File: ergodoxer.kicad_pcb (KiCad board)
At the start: 2 copper layers, 197.9 x 173.2 mm, 163 parts, among them J1 USB_C_Receptacle, SW1 SW_Push_mod, SW10 SW_Push, SW11 SW_Push, SW12 SW_Push, SW13 SW_Push_mod, SW14 SW_Push, SW15 SW_Push, SW16 SW_Push, SW17 SW_Push, SW18 SW_Push, SW19 SW_Push_mod, SW2 SW_Push, SW20 SW_Push, SW21 SW_Push, SW22 SW_Push, SW23 SW_Push, SW24 SW_Push, SW25 SW_Push_mod, SW26 SW_Push, SW27 SW_Push, SW28 SW_Push, SW29 SW_Push, SW3 SW_Push, SW30 SW_Push, SW31 SW_Push_mod, SW32 SW_Push, SW33 SW_Push, SW34 SW_Push, SW35 SW_Push, SW37 SW_Push_mod, SW38 SW_Push, SW39 SW_Push, SW4 SW_Push, SW40 SW_Push, SW41 SW_Push, SW43 SW_Push, SW45 SW_Push, SW46 SW_Push, SW48 SW_Push, SW49 SW_Push, SW5 SW_Push, SW50 SW_Push, SW51 SW_Push, SW52 SW_Push, SW53 SW_Push, SW6 SW_Push, SW7 SW_Push_mod, SW8 SW_Push, SW9 SW_Push, U1 proton_c

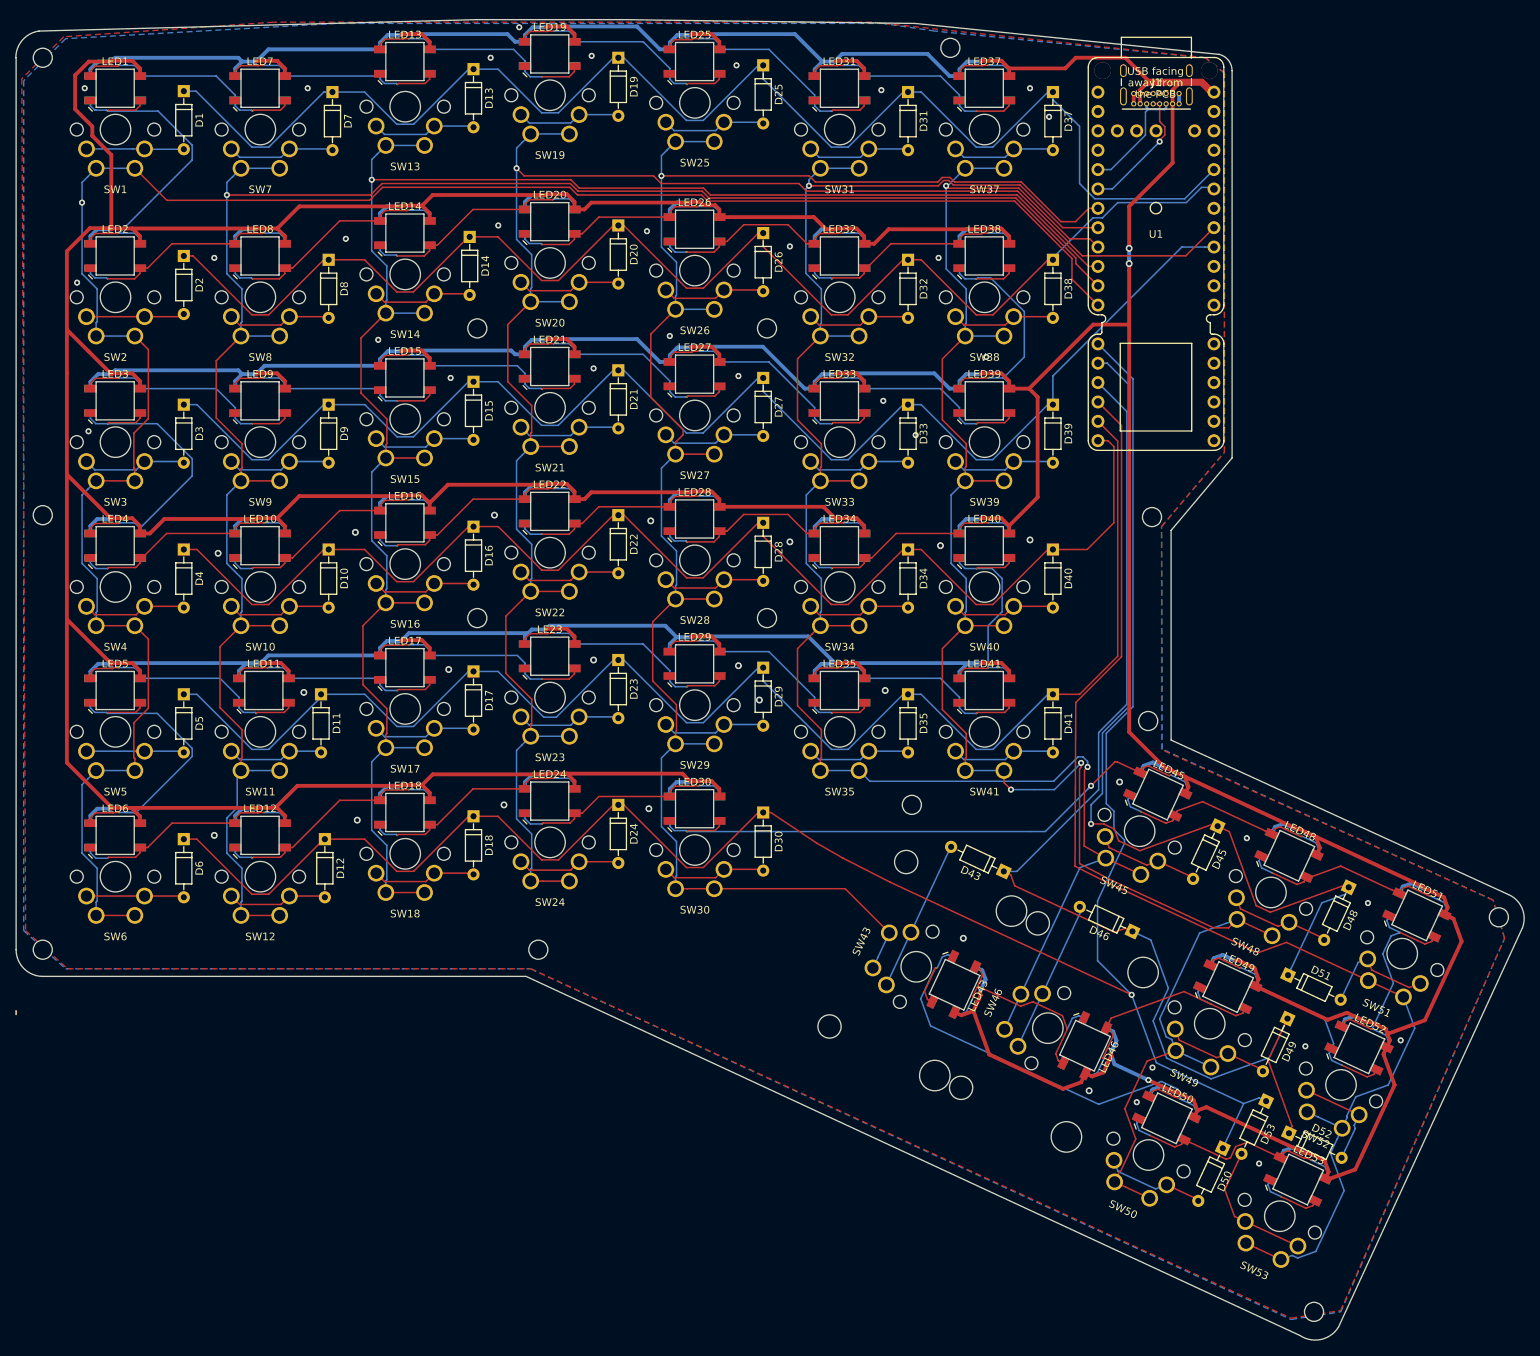
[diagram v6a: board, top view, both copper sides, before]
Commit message: Change microcontroller to neutron c
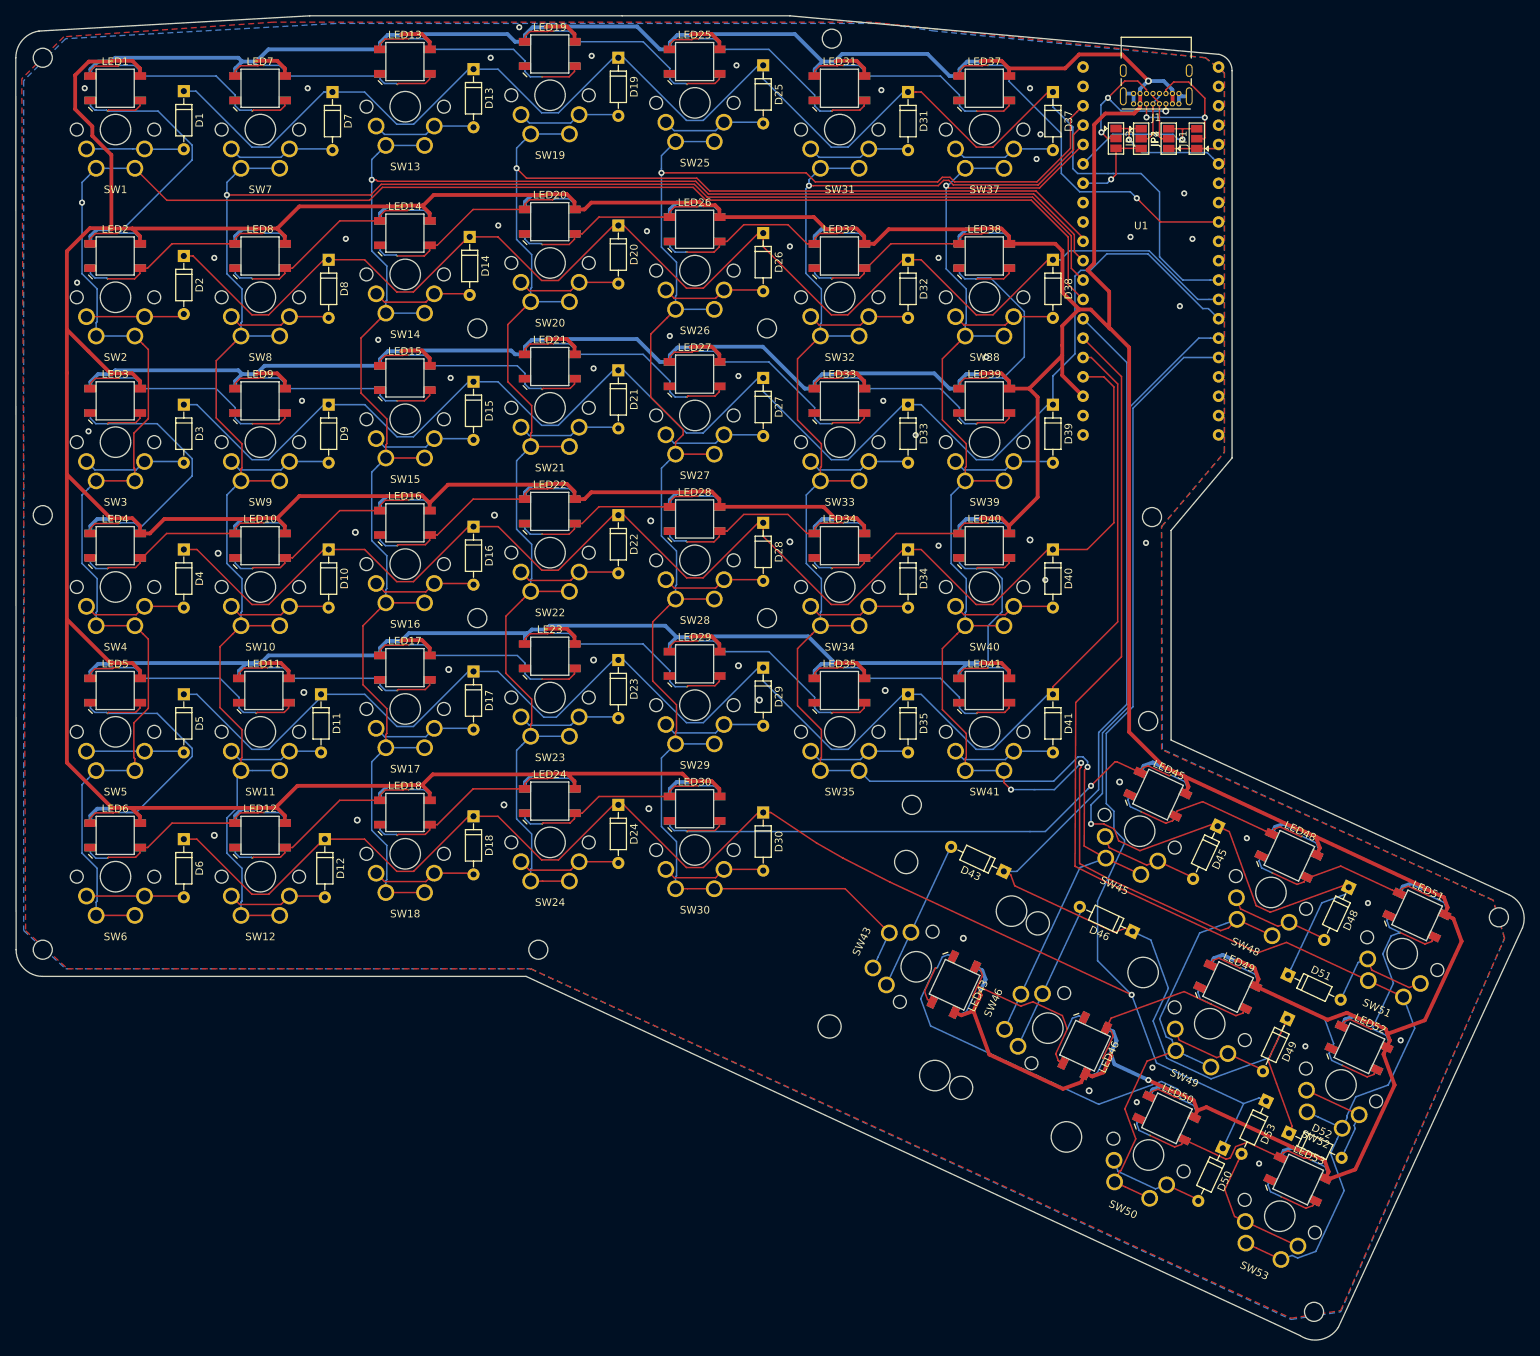
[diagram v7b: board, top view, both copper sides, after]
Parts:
- added JP1: SolderJumper_3_Open, Jumper:SolderJumper-3_P1.3mm_Open_Pad1.0x1.5mm, F.Cu at (218.4, 35.1)
- added JP2: SolderJumper_3_Open, Jumper:SolderJumper-3_P1.3mm_Open_Pad1.0x1.5mm, F.Cu at (214.7, 35.1)
- added JP3: SolderJumper_3_Open, Jumper:SolderJumper-3_P1.3mm_Open_Pad1.0x1.5mm, F.Cu at (207.8, 35.1)
- added JP4: SolderJumper_3_Open, Jumper:SolderJumper-3_P1.3mm_Open_Pad1.0x1.5mm, F.Cu at (211.1, 35.1)
- J1: value USB_C_Receptacle -> USB_C_Receptacle_USB2.0
- U1: value proton_c -> neutron-c; footprint protonc:proton_c -> neutron-c:neutron-c
- moved REF** 15.6 mm to (170.5, 22.0)
- moved U1 2.63 mm to (211.1, 46.0)
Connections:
- J1 pad A5: SDA -> SBU
- J1 pad A6: SCL -> D+
- J1 pad A7: SCL -> D-
- J1 pad A8: SDA -> CC
- J1 pad B5: Net-(J1-PadB5) -> SBU
- J1 pad B6: Net-(J1-PadB6) -> D+
- J1 pad B7: Net-(J1-PadB7) -> D-
- J1 pad B8: Net-(J1-PadB8) -> CC
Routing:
- net ledinput: track 8.48 -> 47.4 mm, vias 0 -> 1
- net SBU: track 0.00 -> 23.4 mm, vias 0 -> 3
- net CC: track 0.00 -> 22.6 mm, vias 0 -> 2
- net uart1_tx: track 0.00 -> 20.0 mm, vias 0 -> 1
- net column4: track 236.6 -> 217.3 mm
- net uart3_tx: track 0.00 -> 17.8 mm, vias 0 -> 1
- net SCL: track 17.0 -> 0.00 mm, vias 1 -> 0
- net SDA: track 15.4 -> 0.00 mm
- net VBUS: track 1472.6 -> 1485.2 mm, vias 3 -> 2
- net uart1_rx: track 0.00 -> 11.5 mm, vias 0 -> 1
- net row4: track 172.8 -> 182.8 mm
- net row3: track 182.8 -> 192.6 mm
- net row8: track 148.7 -> 157.9 mm
- net column8: track 166.5 -> 175.6 mm
- net row1: track 184.5 -> 192.3 mm
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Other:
- board size 197.9 x 173.2 mm -> 197.9 x 173.7 mm
